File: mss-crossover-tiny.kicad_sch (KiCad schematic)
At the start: 31 parts, among them J1 RJ45, J2 RJ45, J3 Screw_Terminal_01x02, J4 Screw_Terminal_01x02, J5 Screw_Terminal_01x02, J6 ISP (5V), J7 Screw_Terminal_01x02, SW1 Set, U1 TLP187, U2 AMS1117-3.3, U3 ATtiny25-20SS, U4 TLP187, U5 INA180A3

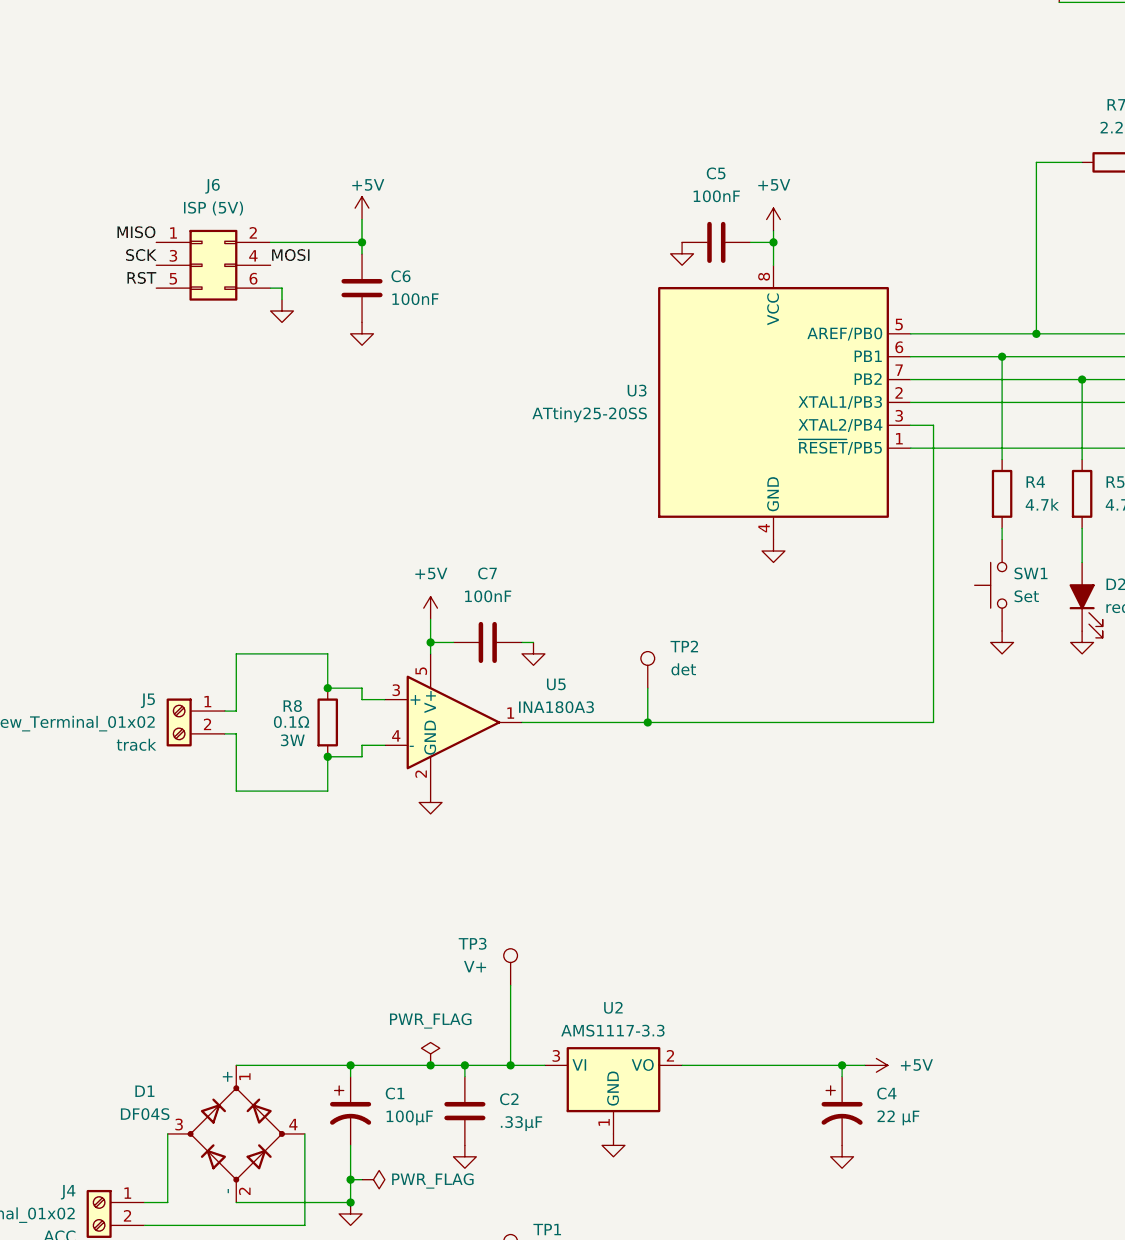
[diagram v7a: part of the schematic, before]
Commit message: Changed everything to 3.3V instead of 5V
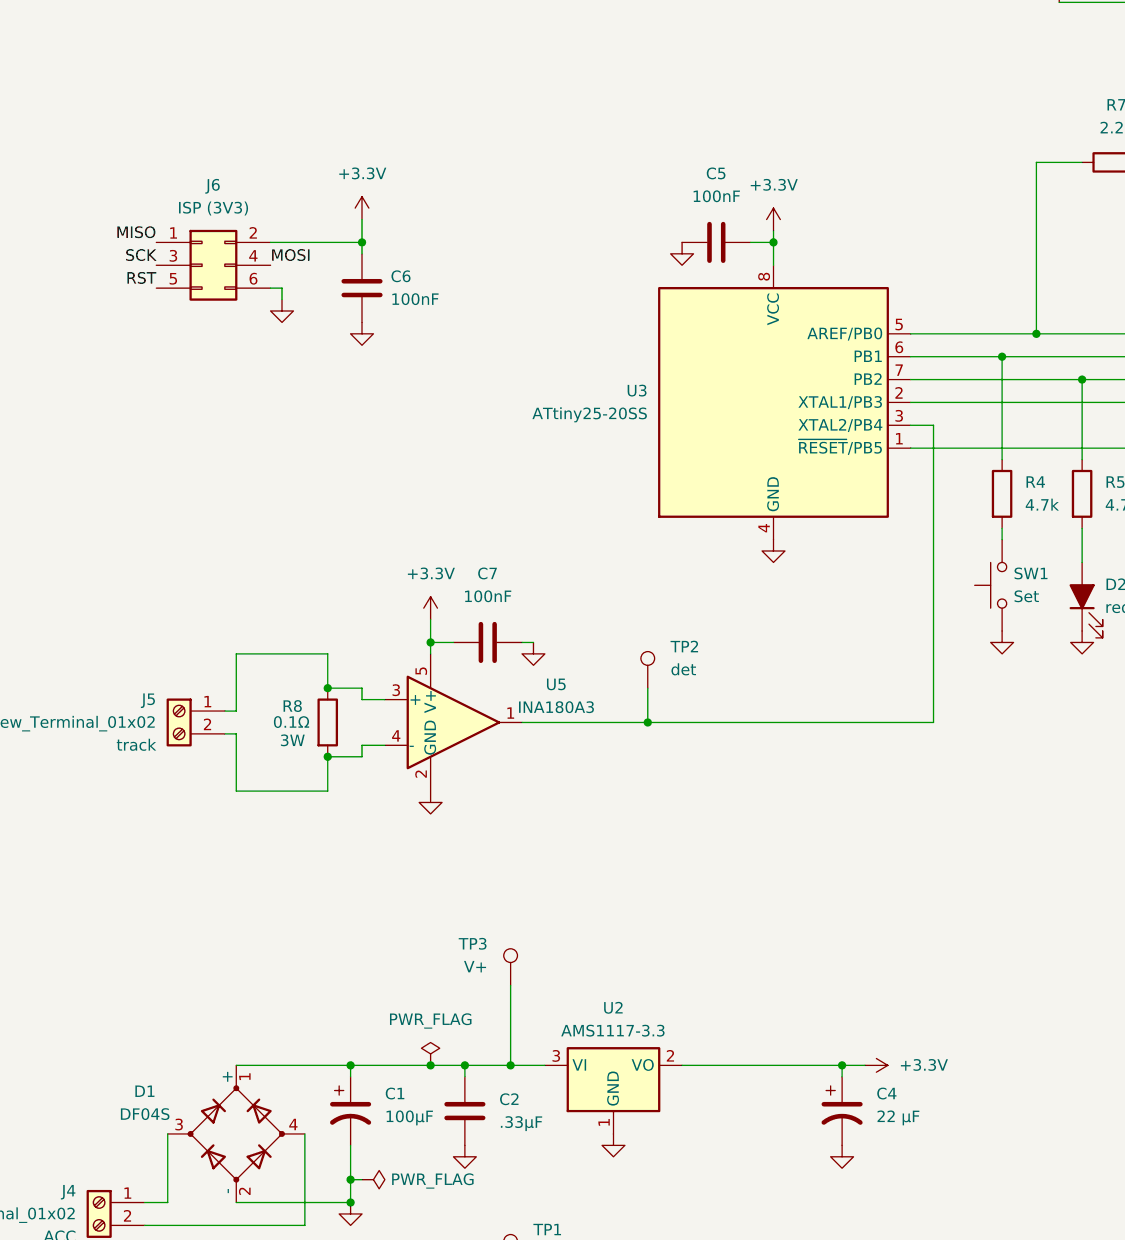
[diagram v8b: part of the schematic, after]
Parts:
- J6: value ISP (5V) -> ISP (3V3)
- SW1: footprint SW_Push_1P1T_NO_CK_KMR2 -> Button_Switch_SMD:SW_Push_1P1T_NO_CK_KMR2; FT Position Offset 5,0 -> 0,.4
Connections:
- net +5V renamed +3.3V
